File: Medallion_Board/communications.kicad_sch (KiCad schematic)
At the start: 18 parts, among them IC1 Wio-SX1262, J4 IPEX, J5 IPEX, U8 LC86LICMD

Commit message: Some minor cleaning
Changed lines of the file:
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@@
 		(title "Smart Compass")
 		(date "2026-06-04")
+		(rev "0.2")
 	)

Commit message: review bom and footprints
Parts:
- C52: value 100mF -> 0.1F
- R20, R22: footprint Resistor_SMD:R_0402_1005Metric -> Resistor_SMD:R_0603_1608Metric

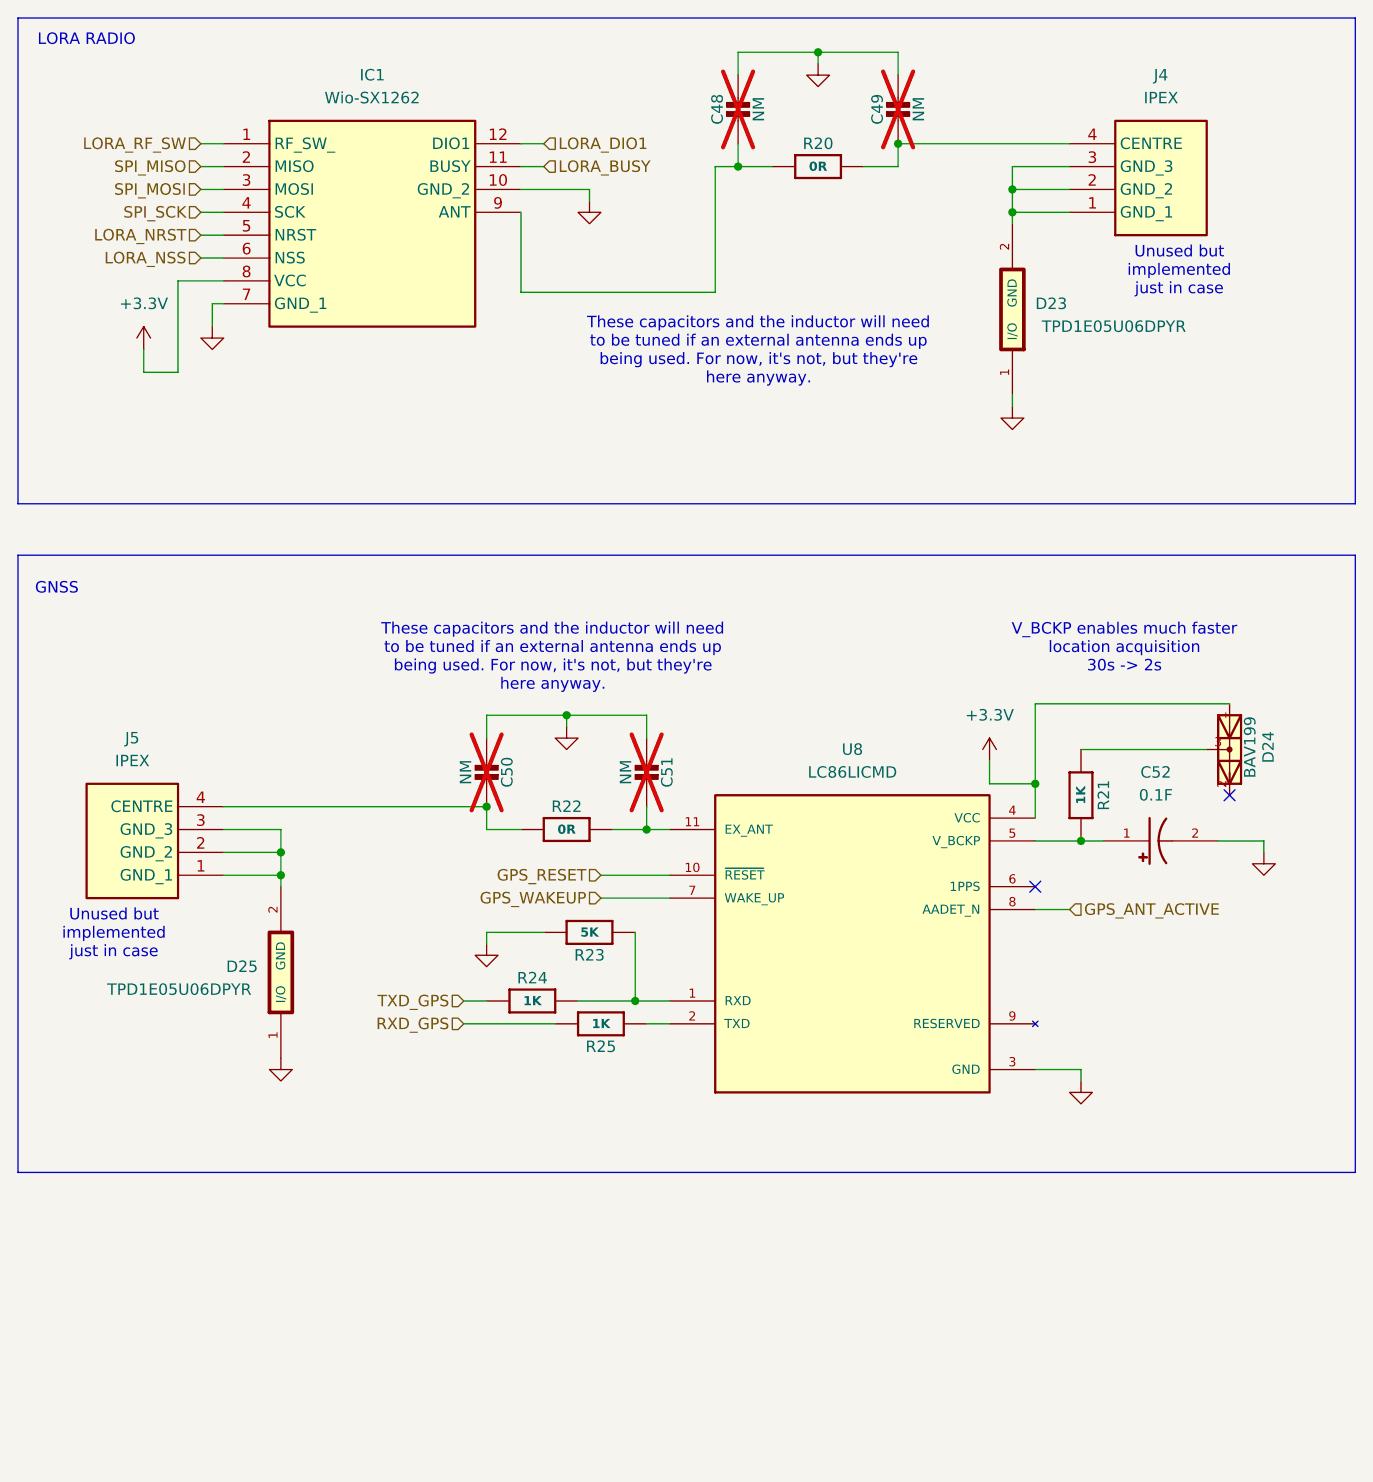
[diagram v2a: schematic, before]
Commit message: Re-did the layout and routing for the whole board. Added more LEDs, haptics, and properly modelled the e-ink display
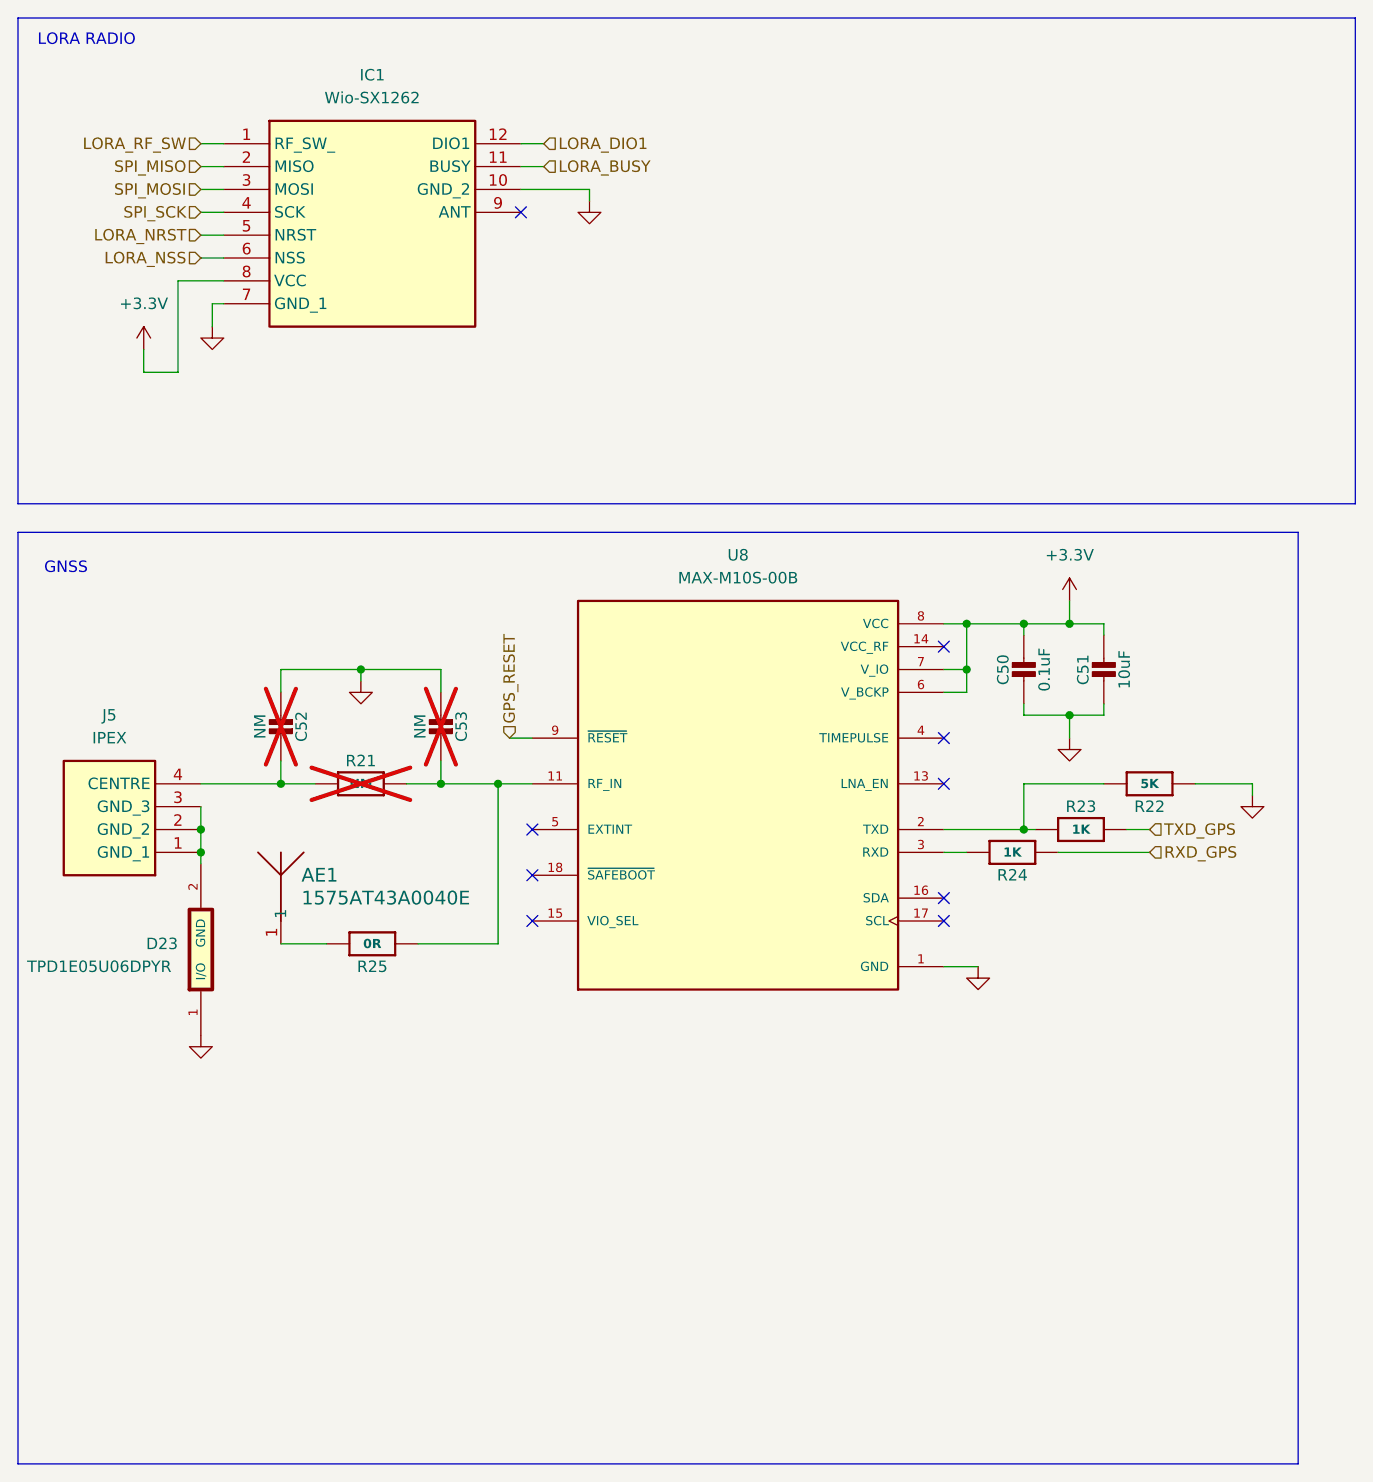
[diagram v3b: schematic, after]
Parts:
- removed C48, C49: NM, Capacitor_SMD:C_0402_1005Metric, symbol Adafruit ESP32-S3 8MB No PSRAM-eagle-import:CAP_CERAMIC0805-NOOUTLINE
- removed C52: 0.1F, KW-5R5C104-R:CAPPRD500W60D1000H3150, symbol XH414HG-IV01E:XH414HG-IV01E
- removed D24: BAV199, BAV199:SOT23, symbol BAV199:BAV199
- removed D25: TPD1E05U06DPYR, TPD1E05U06DPYR:DIO_TPD1E05U06DPYR, symbol TPD1E05U06DPYR:TPD1E05U06DPYR
- removed J4: IPEX, RECE.20369:RECE20369001E01, symbol RECE_20369_001E_01:RECE.20369.001E.01
- removed R20: 0R, Resistor_SMD:R_0603_1608Metric, symbol Adafruit ESP32-S3 8MB No PSRAM-eagle-import:RESISTOR_0603_NOOUT
- removed U8: LC86LICMD, LC86LICMD:MODULE_LC86LICMD, symbol LC86LICMD:LC86LICMD
- added AE1: 1575AT43A0040E, 1575AT43A0040E:ANT_1575AT_JOT, symbol 2026-06-05_23-02-22:1575AT43A0040E
- added C52, C53: NM, Capacitor_SMD:C_0402_1005Metric, symbol Adafruit ESP32-S3 8MB No PSRAM-eagle-import:CAP_CERAMIC0805-NOOUTLINE
- added U8: MAX-M10S-00B, MAX-M10S-00B:XCVR_MAX-M10S-00B, symbol MAX-M10S-00B:MAX-M10S-00B
- C50: value NM -> 0.1uF; MPN (none) -> 0402B104K160HI; PRICE (none) -> 0.02134; now fitted
- C51: value NM -> 10uF; footprint Capacitor_SMD:C_0402_1005Metric -> Capacitor_SMD:C_0805_2012Metric; MPN (none) -> CL21A106KPFNNNG; PRICE (none) -> 0.07; now fitted
- R21: value 1K -> NM; MPN RC0603FR-071KL -> (none); PRICE 0.07 -> (none); now not fitted
- R22: value 0R -> 5K
- R23: value 5K -> 1K; MPN RT0603BRE075KL -> RC0603FR-071KL
- R25: value 1K -> 0R; MPN RC0603FR-071KL -> RT0603BRE075KL
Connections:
- net +3.3V: now also C50.1, C51.1, U8.6 (V_BCKP), U8.7 (V_IO), U8.8 (VCC)
- net GND: now also R22.2, C52.2, C53.2, U8.1 (GND), U8.10 (GND), U8.12 (GND); no longer R23.2
- net GPS_RESET: now also U8.9 (~{RESET})
- net RXD_GPS: now also R24.2; no longer R25.2
- net TXD_GPS: now also R23.1; no longer R24.1
- net at R21.1: now also J5.4 (CENTRE), C52.1
- net at R21.2: now also R25.1, C53.1, U8.11 (RF_IN)
- net at D23.2 (GND): now also J5.1 (GND_1), J5.2 (GND_2), J5.3 (GND_3)
- new net: R22.1, R23.2, U8.2 (TXD)
- new net: R24.1, U8.3 (RXD)
- new net: AE1.1, R25.2
- no-connect marks 2 -> 9
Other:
- note removed: "These capacitors and the inductor will need to be tuned if an external antenna ends up being used. For now, it's not, but they're here anyway."
- note removed: "Unused but implemented just in case"
- note removed: "V_BCKP enables much faster location acquisition 30s -> 2s"
